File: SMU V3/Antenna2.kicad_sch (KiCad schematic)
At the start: 9 parts, among them J4 SMA

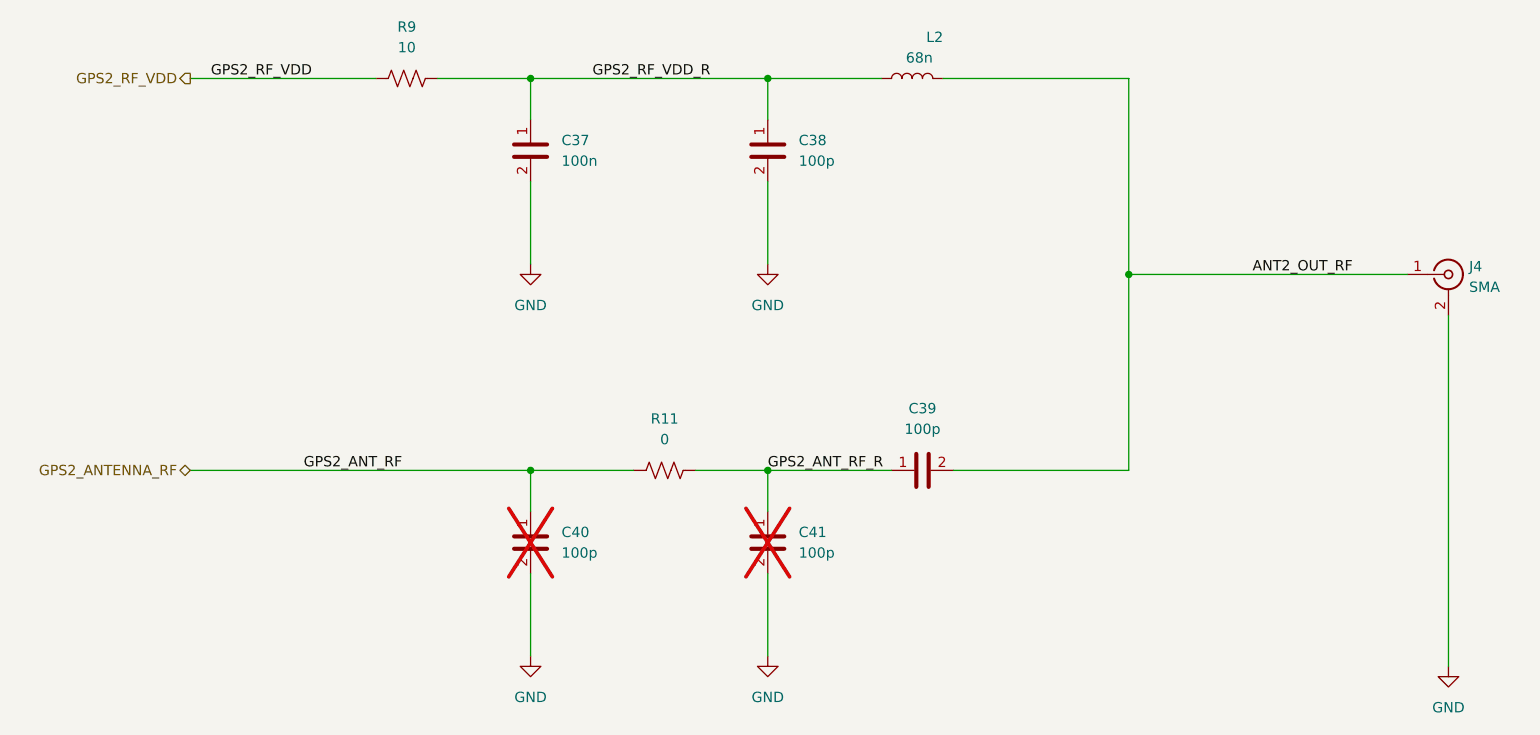
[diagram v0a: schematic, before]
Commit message: improved V3
added uart/spi test points and status leds
removed main 3v3 ldo
added silkscreen
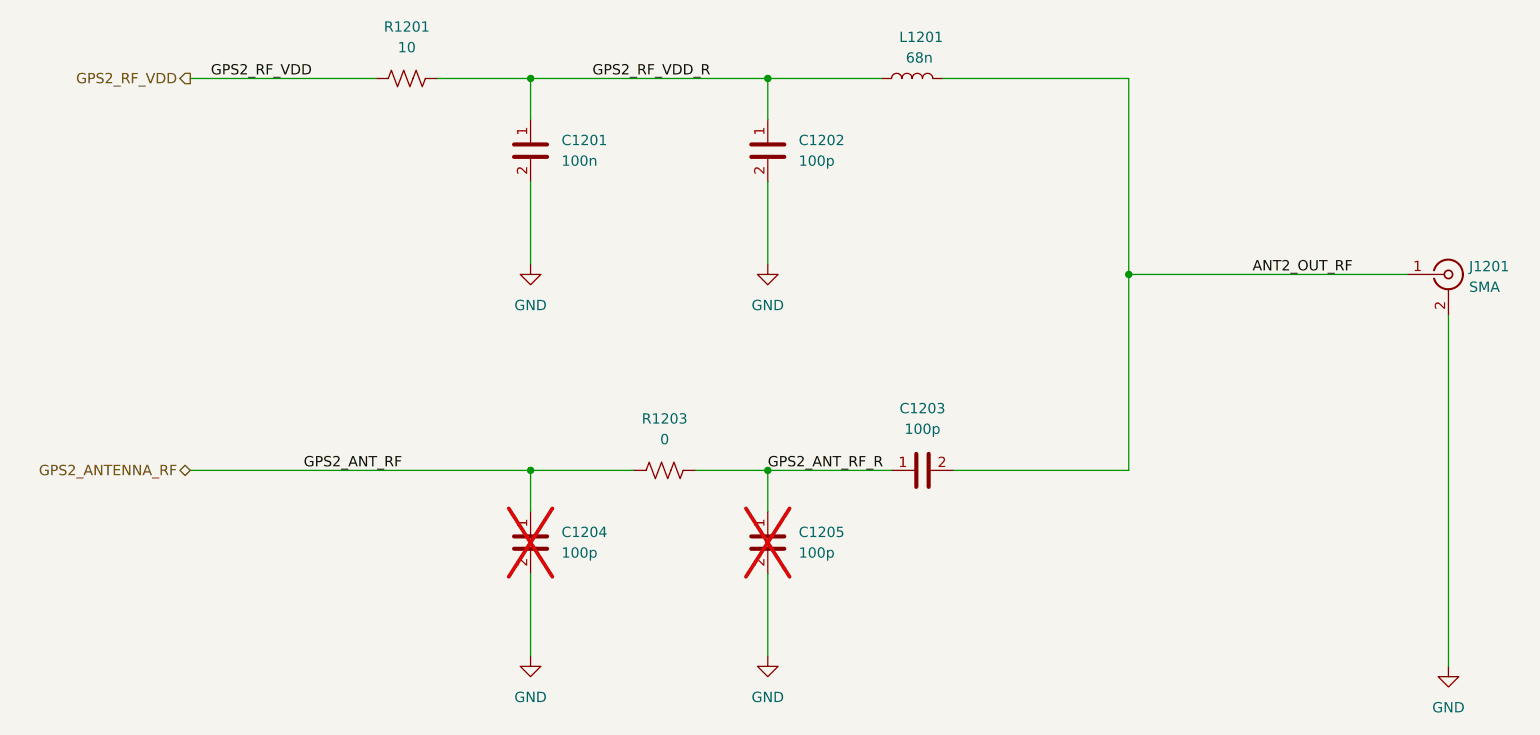
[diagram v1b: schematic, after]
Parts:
- renumbered C37 to C1201, C38 to C1202, C39 to C1203, C40 to C1204, C41 to C1205, J4 to J1201, L2 to L1201, R9 to R1201, R11 to R1203
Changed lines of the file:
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@@
 		(dnp yes)
 		(fields_autoplaced yes)
-		(property "Reference" "C41"
+		(property "Reference" "C1205"
 			(at 149.86 109.2199 0)
 			(show_name no)
@@
 			(project "SMU V3"
 				(path "/1f58b889-96e6-4877-90a3-5a655db5910b/8b50222f-294b-480b-a2b8-7223fbb1c8b6"
-					(reference "C41")
+					(reference "C1205")
 					(unit 1)
 				)
@@
 		(dnp no)
 		(fields_autoplaced yes)
-		(property "Reference" "R9"
+		(property "Reference" "R1201"
 			(at 101.6 46.99 0)
 			(show_name no)
@@
 			(project "SMU V3"
 				(path "/1f58b889-96e6-4877-90a3-5a655db5910b/8b50222f-294b-480b-a2b8-7223fbb1c8b6"
-					(reference "R9")
+					(reference "R1201")
 					(unit 1)
 				)
@@
 		(dnp no)
 		(fields_autoplaced yes)
-		(property "Reference" "C39"
+		(property "Reference" "C1203"
 			(at 165.1 93.98 90)
 			(show_name no)
@@
 			(project "SMU V3"
 				(path "/1f58b889-96e6-4877-90a3-5a655db5910b/8b50222f-294b-480b-a2b8-7223fbb1c8b6"
-					(reference "C39")
+					(reference "C1203")
 					(unit 1)
 				)
@@
 		(dnp no)
 		(fields_autoplaced yes)
-		(property "Reference" "J4"
+		(property "Reference" "J1201"
 			(at 232.41 76.4931 0)
 			(show_name no)
@@
 			(project "SMU V3"
 				(path "/1f58b889-96e6-4877-90a3-5a655db5910b/8b50222f-294b-480b-a2b8-7223fbb1c8b6"
-					(reference "J4")
+					(reference "J1201")
 					(unit 1)
 				)
@@
 		(dnp no)
 		(fields_autoplaced yes)
-		(property "Reference" "R11"
+		(property "Reference" "R1203"
 			(at 133.35 95.25 0)
 			(show_name no)
@@
 			(project "SMU V3"
 				(path "/1f58b889-96e6-4877-90a3-5a655db5910b/8b50222f-294b-480b-a2b8-7223fbb1c8b6"
-					(reference "R11")
+					(reference "R1203")
 					(unit 1)
 				)
@@
 		(in_pos_files yes)
 		(dnp no)
-		(property "Reference" "L2"
+		(property "Reference" "L1201"
 			(at 167.64 48.26 0)
 			(show_name no)
@@
 			(project "SMU V3"
 				(path "/1f58b889-96e6-4877-90a3-5a655db5910b/8b50222f-294b-480b-a2b8-7223fbb1c8b6"
-					(reference "L2")
+					(reference "L1201")
 					(unit 1)
 				)
@@
 		(dnp no)
 		(fields_autoplaced yes)
-		(property "Reference" "C38"
+		(property "Reference" "C1202"
 			(at 149.86 60.9599 0)
 			(show_name no)
@@
 			(project "SMU V3"
 				(path "/1f58b889-96e6-4877-90a3-5a655db5910b/8b50222f-294b-480b-a2b8-7223fbb1c8b6"
-					(reference "C38")
+					(reference "C1202")
 					(unit 1)
 				)
@@
 		(dnp no)
 		(fields_autoplaced yes)
-		(property "Reference" "C37"
+		(property "Reference" "C1201"
 			(at 120.65 60.9599 0)
 			(show_name no)
@@
 			(project "SMU V3"
 				(path "/1f58b889-96e6-4877-90a3-5a655db5910b/8b50222f-294b-480b-a2b8-7223fbb1c8b6"
-					(reference "C37")
+					(reference "C1201")
 					(unit 1)
 				)
@@
 		(dnp no)
 		(fields_autoplaced yes)
-		(property "Reference" "#PWR036"
+		(property "Reference" "#PWR01206"
 			(at 146.05 130.81 0)
 			(hide yes)
@@
 			(project "SMU V3"
 				(path "/1f58b889-96e6-4877-90a3-5a655db5910b/8b50222f-294b-480b-a2b8-7223fbb1c8b6"
-					(reference "#PWR036")
+					(reference "#PWR01206")
 					(unit 1)
 				)
@@
 		(dnp no)
 		(fields_autoplaced yes)
-		(property "Reference" "#PWR038"
+		(property "Reference" "#PWR01207"
 			(at 229.87 132.08 0)
 			(hide yes)
@@
 			(project "SMU V3"
 				(path "/1f58b889-96e6-4877-90a3-5a655db5910b/8b50222f-294b-480b-a2b8-7223fbb1c8b6"
-					(reference "#PWR038")
+					(reference "#PWR01207")
 					(unit 1)
 				)
@@
 		(dnp no)
 		(fields_autoplaced yes)
-		(property "Reference" "#PWR032"
+		(property "Reference" "#PWR01202"
 			(at 116.84 82.55 0)
 			(hide yes)
@@
 			(project "SMU V3"
 				(path "/1f58b889-96e6-4877-90a3-5a655db5910b/8b50222f-294b-480b-a2b8-7223fbb1c8b6"
-					(reference "#PWR032")
+					(reference "#PWR01202")
 					(unit 1)
 				)
@@
 		(dnp no)
 		(fields_autoplaced yes)
-		(property "Reference" "#PWR035"
+		(property "Reference" "#PWR01203"
 			(at 146.05 82.55 0)
 			(hide yes)
@@
 			(project "SMU V3"
 				(path "/1f58b889-96e6-4877-90a3-5a655db5910b/8b50222f-294b-480b-a2b8-7223fbb1c8b6"
-					(reference "#PWR035")
+					(reference "#PWR01203")
 					(unit 1)
 				)
@@
 		(dnp no)
 		(fields_autoplaced yes)
-		(property "Reference" "#PWR033"
+		(property "Reference" "#PWR01205"
 			(at 116.84 130.81 0)
 			(hide yes)
@@
 			(project "SMU V3"
 				(path "/1f58b889-96e6-4877-90a3-5a655db5910b/8b50222f-294b-480b-a2b8-7223fbb1c8b6"
-					(reference "#PWR033")
+					(reference "#PWR01205")
 					(unit 1)
 				)
@@
 		(dnp yes)
 		(fields_autoplaced yes)
-		(property "Reference" "C40"
+		(property "Reference" "C1204"
 			(at 120.65 109.2199 0)
 			(show_name no)
@@
 			(project "SMU V3"
 				(path "/1f58b889-96e6-4877-90a3-5a655db5910b/8b50222f-294b-480b-a2b8-7223fbb1c8b6"
-					(reference "C40")
+					(reference "C1204")
 					(unit 1)
 				)
